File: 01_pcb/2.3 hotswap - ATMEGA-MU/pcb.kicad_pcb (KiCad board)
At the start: 2 copper layers, 251.2 x 75 mm, 128 parts, among them J1 TYPE-C-31-M12_13, J2 AVR-ISP-6_mod, J3 Conn_01x08, J8 4PIN, SW1 SW_PUSH, U2 PRTR5V0U2X, U3 ATmega32U4-M, Y1 16MHz

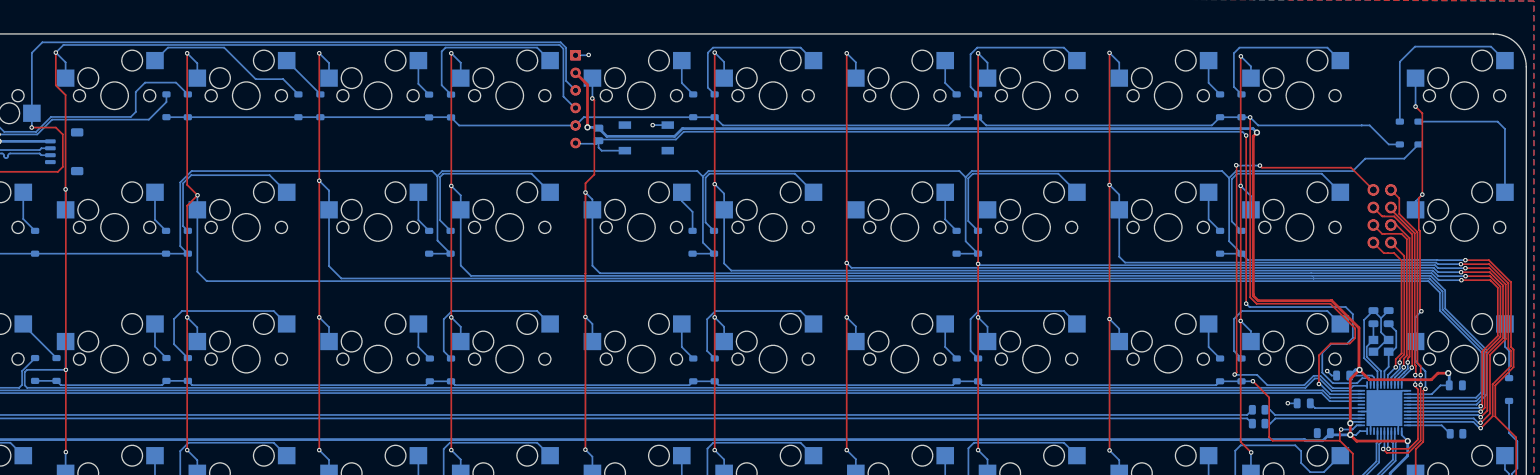
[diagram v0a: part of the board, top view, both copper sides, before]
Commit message: added ATMEGA-MU MCU
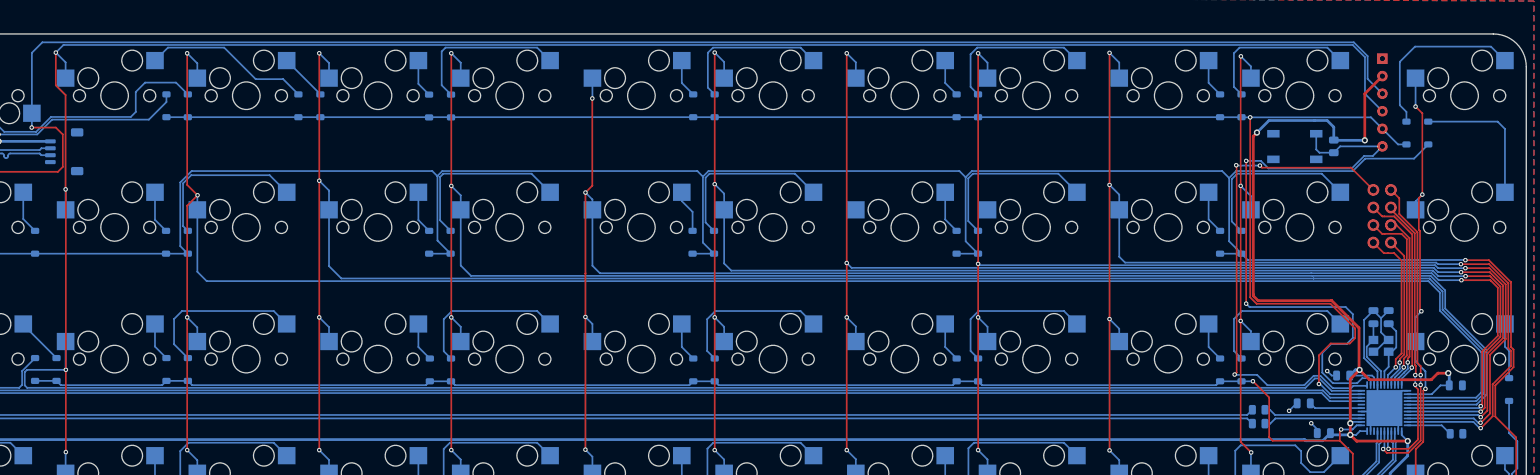
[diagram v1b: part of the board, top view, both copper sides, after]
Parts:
- moved J2 116.7 mm to (308.4, 54.2)
- moved RSW1 106.4 mm to (301.3, 60.5)
- moved SW1 93.8 mm to (295.7, 60.5), turned to 180 degrees
- moved D26 1.41 mm to (315.0, 58.6)
- moved D13 0.96 mm to (311.9, 58.6)
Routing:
- net col1/sck: track 382.3 -> 498.3 mm
- net col2/miso: track 359.1 -> 475.0 mm
- net VCC: track 492.2 -> 414.5 mm
- net ISP_Reset: track 163.5 -> 91.0 mm
- net GND: track 63.8 -> 61.7 mm, vias 5 -> 4
- net row0/mosi: track 244.6 -> 242.6 mm
- net Net-(D26-A): track 22.1 -> 20.7 mm
- net row1: track 418.0 -> 419.4 mm
